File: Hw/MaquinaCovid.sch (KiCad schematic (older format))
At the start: 44 parts, among them J1 5 VCC, J10 Conn_01x04, J2 HC-SR04, J3 FTDI, J4 LCD, J5 MLX90614, J6 DS1307, J7 SD, J8 Power_supply, J9 Pines adicionales, Q1 2N2219, Q2 2N2219, SW1 RST, SW2 BOOT, SW3 SW_Push, U1 AZ1084CD-5.0TRG1, U2 AP2114H-3.3TRG1, U3 ESP32-WROOM-32, U4 LTV-817, U5 LTV-817, Y1 UD2-3NU

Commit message: Schematic changes
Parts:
- added R? (x2): 3.3k, symbol Device:R
- Q1: value 2N2219 -> MMBT4403; symbol Transistor_BJT:2N2219 -> agroin:MMBT2222A
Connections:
- net +3V3: now also J2.1 (Pin_1), J3.4 (Pin_4), J5.1 (Pin_1), J6.5 (Pin_5), J7.5 (Pin_5), R?.1, R?.1
- net +5V: no longer J2.1 (Pin_1), J3.4 (Pin_4), J5.1 (Pin_1), J6.5 (Pin_5), J7.5 (Pin_5)
- net GND: now also Q1.2 (E); no longer Q1.1 (E)
- net SCL: now also R?.2
- net SDA: now also R?.2
- net at R1.1: now also Q1.1 (B); no longer Q1.2 (B)
- net DS: no longer names the net of J6.2 (Pin_2)
- net GPIO2: no longer names the net of U3.26 (IO4)
- net SQ: no longer names the net of J6.1 (Pin_1)
- no-connect marks 13 -> 16
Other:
- moved on the sheet: C5, D4, D5, D6, R2, R3, R5

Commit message: finished Schematic
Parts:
- removed J1: 5 VCC, TerminalBlock:TerminalBlock_bornier-2_P5.08mm, symbol Connector:Screw_Terminal_01x02
- removed J10: Conn_01x04, symbol Connector_Generic:Conn_01x03
- removed J8: Power_supply, symbol Connector_Generic:Conn_01x02
- removed J9: Pines adicionales, symbol Connector_Generic:Conn_01x10
- removed Q2: 2N2219, Package_TO_SOT_THT:TO-39-3, symbol Transistor_BJT:2N2219
- removed R5: 330, symbol Device:R
- added D8: FM4007W-W, agroin:F4007, symbol Device:D
- added J10, J11: Screw_Terminal_01x03, TerminalBlock:TerminalBlock_bornier-3_P5.08mm, symbol Connector:Screw_Terminal_01x03
- added J7: Screw_Terminal_01x02, TerminalBlock:TerminalBlock_bornier-2_P5.08mm, symbol Connector:Screw_Terminal_01x02
- added J8, J9: Screw_Terminal_01x11, TerminalBlock:TerminalBlock_bornier-6_P5.08mm, symbol Connector:Screw_Terminal_01x06
- added Q2, Q3: MMBT2222A, Package_TO_SOT_SMD:SOT-23, symbol Transistor_BJT:2N3055
- added R12: 1k, Resistor_SMD:R_0805_2012Metric_Pad1.15x1.40mm_HandSolder, symbol Device:R
- added R4: 330, Resistor_SMD:R_0805_2012Metric_Pad1.15x1.40mm_HandSolder, symbol Device:R
- added Y1: UD2-3NU, agroin:UD2-3NU, symbol agroin:UD2-3NU
- BZ1: footprint (none) -> agroin:Buzzer
- D1, D3: value D_Schottky -> SS24FL; footprint (none) -> Diode_SMD:D_SOD-123F
- D2: value D -> 1N4148; footprint (none) -> Diode_SMD:D_SOD-323
- D4, D5, D6: footprint (none) -> LED_THT:LED_D10.0mm
- D7: value D -> FM4007W-W; footprint (none) -> agroin:F4007
- J1: renamed from J2; footprint (none) -> Connector_PinHeader_2.54mm:PinHeader_1x04_P2.54mm_Vertical
- J2: renamed from J3; footprint (none) -> Connector_PinHeader_2.54mm:PinHeader_1x06_P2.54mm_Vertical
- J3: renamed from J4; footprint (none) -> Connector_PinHeader_2.54mm:PinHeader_1x04_P2.54mm_Vertical
- J4: renamed from J5; footprint (none) -> Connector_PinHeader_2.54mm:PinHeader_1x04_P2.54mm_Vertical
- J5: renamed from J6; footprint (none) -> Connector_PinHeader_2.54mm:PinHeader_1x06_P2.54mm_Vertical
- J6: renamed from J7; footprint (none) -> Connector_PinHeader_2.54mm:PinHeader_1x06_P2.54mm_Vertical
- Q1: value MMBT4403 -> MMBT2222A; footprint Package_TO_SOT_THT:TO-39-3 -> Package_TO_SOT_SMD:SOT-23
- R1, R2, R3: footprint (none) -> Resistor_SMD:R_0805_2012Metric_Pad1.15x1.40mm_HandSolder
- R10: renamed from R8; footprint (none) -> Resistor_SMD:R_0805_2012Metric_Pad1.15x1.40mm_HandSolder
- R11: renamed from R9; footprint (none) -> Resistor_SMD:R_0805_2012Metric_Pad1.15x1.40mm_HandSolder
- R13: renamed from R10; footprint (none) -> Resistor_SMD:R_0805_2012Metric_Pad1.15x1.40mm_HandSolder
- R6, R7: renamed from R?; footprint (none) -> Resistor_SMD:R_0805_2012Metric_Pad1.15x1.40mm_HandSolder
- R8: renamed from R6; footprint (none) -> Resistor_SMD:R_0805_2012Metric_Pad1.15x1.40mm_HandSolder
- R9: renamed from R7; footprint (none) -> Resistor_SMD:R_0805_2012Metric_Pad1.15x1.40mm_HandSolder
- SW3: value SW_Push -> Extra; footprint (none) -> Button_Switch_SMD:SW_SPST_TL3342; lscs# (none) -> C318893; manf# (none) -> TS-1185EC-C-D-B
- U4, U5: footprint Housings_DIP:DIP-4_W7.62mm -> Package_DIP:DIP-4_W7.62mm_Socket
- Y2: renamed from Y1; footprint (none) -> agroin:UD2-3NU
- renumbered R4 to R5
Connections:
- net +3V3: now also D8.1 (K), Y1.8 (C1); no longer J5.5 (Pin_5), J6.5 (Pin_5)
- net +5V: now also J5.5 (Pin_5), J6.5 (Pin_5), J8.1 (Pin_1)
- net GND: now also J7.2 (Pin_2), J8.2 (Pin_2), J9.3 (Pin_3), J9.5 (Pin_5), J9.6 (Pin_6), Q2.2 (E), Q3.2 (E)
- net GPIO: now also J9.1 (Pin_1)
- net L3: now also R4.1
- net OP1: now also J9.2 (Pin_2)
- net OP2: now also J9.4 (Pin_4)
- net PS: now also J7.1 (Pin_1)
- net RX2: now also J8.4 (Pin_4)
- net SCL: now also J8.6 (Pin_6)
- net SDA: now also J8.5 (Pin_5)
- net TX2: now also J8.3 (Pin_3)
- net Ry2: now reaches U3.26 (IO4)
- net Ry2: now also R12.2
- net at D7.2 (A), Y2.1 (C2): now also Q3.3 (C)
- net at R13.1: now also Q3.1 (B)
- net at D6.2 (A): now also R4.2
- net COM renamed COM1
- net COM1: now also J10.2 (Pin_2)
- net NC renamed NC1
- net NC1: now also J10.1 (Pin_1)
- net NO renamed NO1
- net NO1: now also J10.3 (Pin_3)
- net Ry renamed Ry1
- new net: D8.2 (A), Q2.3 (C), Y1.1 (C2)
- new net: Q2.1 (B), R12.1
- new net COM2: J11.2 (Pin_2), Y1.3 (Com), Y1.6 (Com2)
- new net NC2: J11.1 (Pin_1), Y1.2 (NC)
- new net NO2: J11.3 (Pin_3), Y1.5 (NA1)
- no-connect marks 16 -> 17

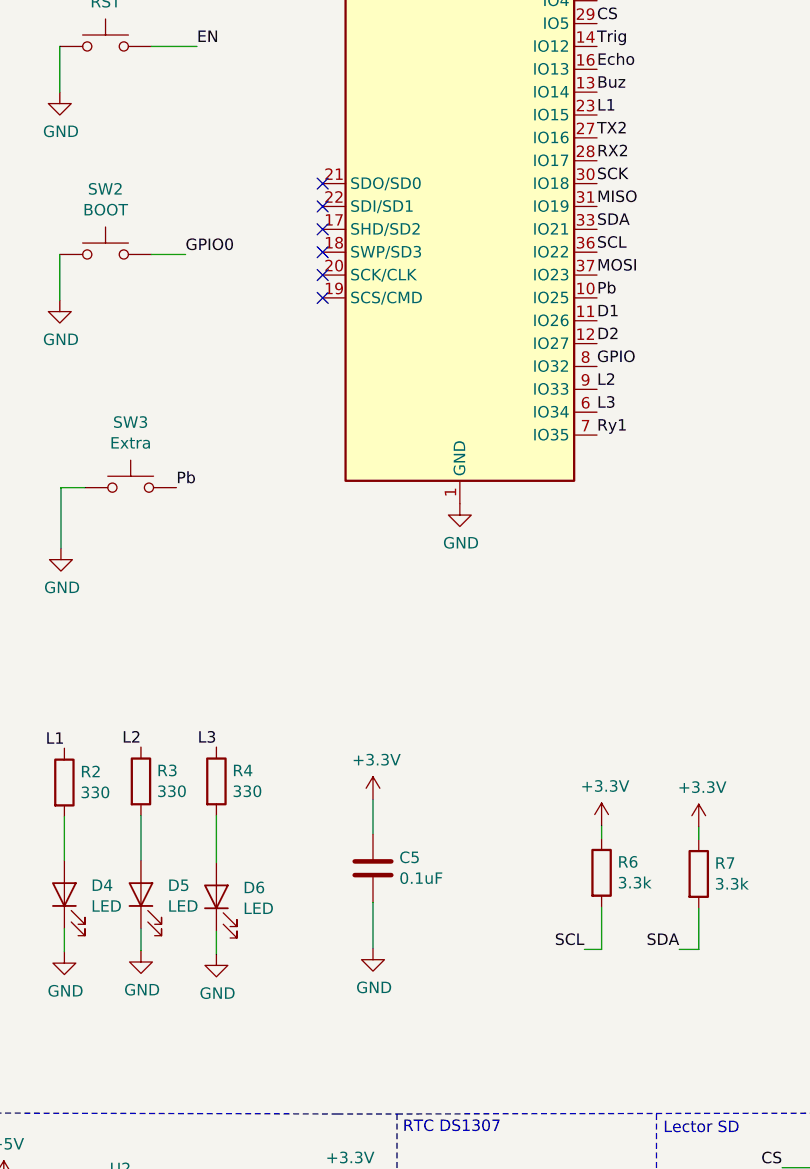
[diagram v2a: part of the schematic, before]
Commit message: Added led
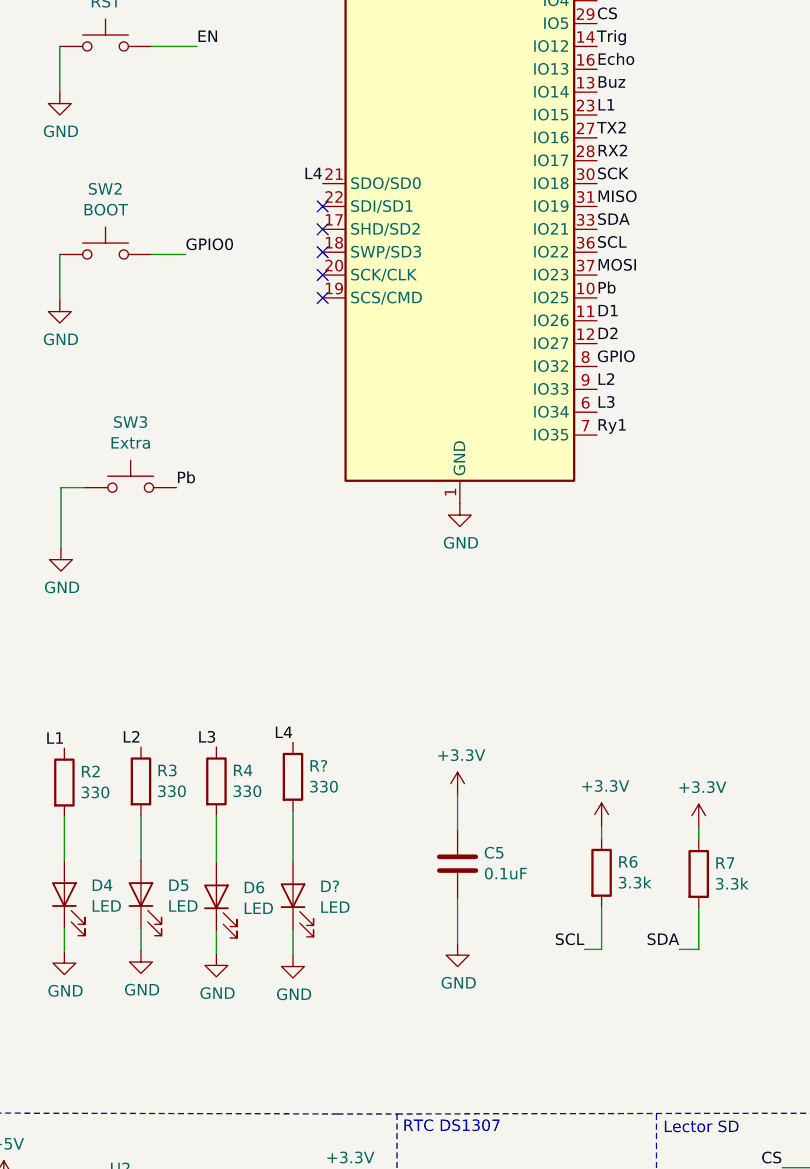
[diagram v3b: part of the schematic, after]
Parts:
- added D?: LED, LED_THT:LED_D10.0mm, symbol Device:LED
- added R?: 330, Resistor_SMD:R_0805_2012Metric_Pad1.15x1.40mm_HandSolder, symbol Device:R
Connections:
- net GND: now also D?.1 (K)
- net L4: now reaches U3.21 (SDO/SD0)
- net L4: now also R?.1
- new net: D?.2 (A), R?.2
- no-connect marks 17 -> 16
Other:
- moved on the sheet: C5
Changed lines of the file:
@@
 L Device:C C5
 U 1 1 5DFBF1D5
-P 4380 5605
-F 0 "C5" H 4495 5651 50  0000 L CNN
-F 1 "0.1uF" H 4495 5560 50  0000 L CNN
-F 2 "Capacitor_SMD:C_0805_2012Metric_Pad1.15x1.40mm_HandSolder" H 4418 5455 50  0001 C CNN
-F 3 "~" H 4380 5605 50  0001 C CNN
-F 4 "C376923" H -3690 3085 50  0001 C CNN "lscs#"
-F 5 "TCC0805X7R104K250DTS" H -3690 3085 50  0001 C CNN "manf#"
-	1    4380 5605
+P 4750 5585
+F 0 "C5" H 4865 5631 50  0000 L CNN
+F 1 "0.1uF" H 4865 5540 50  0000 L CNN
+F 2 "Capacitor_SMD:C_0805_2012Metric_Pad1.15x1.40mm_HandSolder" H 4788 5435 50  0001 C CNN
+F 3 "~" H 4750 5585 50  0001 C CNN
+F 4 "C376923" H -3320 3065 50  0001 C CNN "lscs#"
+F 5 "TCC0805X7R104K250DTS" H -3320 3065 50  0001 C CNN "manf#"
+	1    4750 5585
 	1    0    0    -1
 $EndComp
@@
 L power:GND #PWR025
 U 1 1 5DFBF1E1
-P 4380 5955
-F 0 "#PWR025" H 4380 5705 50  0001 C CNN
-F 1 "GND" H 4385 5782 50  0000 C CNN
-F 2 "" H 4380 5955 50  0001 C CNN
-F 3 "" H 4380 5955 50  0001 C CNN
-	1    4380 5955
-	1    0    0    -1
-$EndComp
-Wire Wire Line
-	4380 5755 4380 5955
-Wire Wire Line
-	4380 5455 4380 5305
+P 4750 5935
+F 0 "#PWR025" H 4750 5685 50  0001 C CNN
+F 1 "GND" H 4755 5762 50  0000 C CNN
+F 2 "" H 4750 5935 50  0001 C CNN
+F 3 "" H 4750 5935 50  0001 C CNN
+	1    4750 5935
+	1    0    0    -1
+$EndComp
+Wire Wire Line
+	4750 5735 4750 5935
+Wire Wire Line
+	4750 5435 4750 5285
 $Comp
 L power:+3.3V #PWR027
@@
 L power:+3.3V #PWR024
 U 1 1 5E03555F
-P 4380 5305
-F 0 "#PWR024" H 4380 5155 50  0001 C CNN
-F 1 "+3.3V" H 4395 5478 50  0000 C CNN
-F 2 "" H 4380 5305 50  0001 C CNN
-F 3 "" H 4380 5305 50  0001 C CNN
-	1    4380 5305
+P 4750 5285
+F 0 "#PWR024" H 4750 5135 50  0001 C CNN
+F 1 "+3.3V" H 4765 5458 50  0000 C CNN
+F 2 "" H 4750 5285 50  0001 C CNN
+F 3 "" H 4750 5285 50  0001 C CNN
+	1    4750 5285
 	1    0    0    -1
 $EndComp
@@
 ESP32
 NoConn ~ 5360 1610
-NoConn ~ 4160 2610
 $Comp
 L power:GND #PWR017
@@
 Wire Wire Line
 	8915 2910 8840 2910
+$Comp
+L Device:R R?
+U 1 1 5F0DC3AE
+P 4030 5205
+F 0 "R?" H 4100 5251 50  0000 L CNN
+F 1 "330" H 4100 5160 50  0000 L CNN
+F 2 "Resistor_SMD:R_0805_2012Metric_Pad1.15x1.40mm_HandSolder" V 3960 5205 50  0001 C CNN
+F 3 "~" H 4030 5205 50  0001 C CNN
+	1    4030 5205
+	1    0    0    -1
+$EndComp
+$Comp
+L Device:LED D?
+U 1 1 5F0DCDF6
+P 4030 5725
+F 0 "D?" V 4069 5608 50  0000 R CNN
+F 1 "LED" V 3978 5608 50  0000 R CNN
+F 2 "LED_THT:LED_D10.0mm" H 4030 5725 50  0001 C CNN
+F 3 "~" H 4030 5725 50  0001 C CNN
+	1    4030 5725
+	0    -1   -1   0
+$EndComp
+Wire Wire Line
+	4030 5355 4030 5575
+$Comp
+L power:GND #PWR?
+U 1 1 5F0E3D15
+P 4030 5985
+F 0 "#PWR?" H 4030 5735 50  0001 C CNN
+F 1 "GND" H 4035 5812 50  0000 C CNN
+F 2 "" H 4030 5985 50  0001 C CNN
+F 3 "" H 4030 5985 50  0001 C CNN
+	1    4030 5985
+	1    0    0    -1
+$EndComp
+Wire Wire Line
+	4030 5985 4030 5875
+Text Label 4030 5055 2    50   ~ 0
+L4
+Text Label 4160 2610 2    50   ~ 0
+L4
 $EndSCHEMATC

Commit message: Footprint placement (part 1)
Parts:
- added H1, H2, H3, H4: MountingHole, MountingHole:MountingHole_3.2mm_M3_Pad_Via, symbol Mechanical:MountingHole
- D7: renamed from D?; footprint LED_THT:LED_D10.0mm -> LED_SMD:LED_0805_2012Metric_Pad1.15x1.40mm_HandSolder
- J5: footprint Connector_PinHeader_2.54mm:PinHeader_1x06_P2.54mm_Vertical -> Connector_PinHeader_2.54mm:PinHeader_1x05_P2.54mm_Vertical; symbol Connector_Generic:Conn_01x06 -> Connector_Generic:Conn_01x05
- gave numbers to parts that had none: 1
- renumbered D7 to D8, D8 to D9, R9 to R10, R10 to R11, R11 to R12, R12 to R13, R13 to R14, R6 to R7, R7 to R8, R8 to R9
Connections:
- net +5V: now also J5.4 (Pin_4); no longer J5.5 (Pin_5)
- net D1: now also U3.8 (IO32); no longer U3.11 (IO26)
- net D2: now also U3.7 (IO35); no longer U3.12 (IO27)
- net GND: now also J5.5 (Pin_5), J7.1 (Pin_1); no longer J5.6 (Pin_6), J7.2 (Pin_2)
- net GPIO: now also U3.9 (IO33); no longer U3.8 (IO32)
- net L2: now also U3.11 (IO26); no longer U3.9 (IO33)
- net L3: now also U3.10 (IO25); no longer U3.6 (IO34)
- net PS: now also J7.2 (Pin_2); no longer J7.1 (Pin_1)
- net Pb: now also U3.6 (IO34); no longer U3.10 (IO25)
- net Ry1: now also U3.12 (IO27); no longer U3.7 (IO35)
- net Ry2: now also U3.17 (SHD/SD2); no longer U3.26 (IO4)
- net SCL: now also J5.2 (Pin_2); no longer J5.3 (Pin_3)
- net SDA: now also J5.3 (Pin_3); no longer J5.4 (Pin_4)
- no-connect marks 16 -> 14

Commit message: Finished PCB
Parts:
- added H5: MountingHole, MountingHole:MountingHole_3.2mm_M3_Pad_Via, symbol Mechanical:MountingHole
- D4, D5, D6: footprint LED_THT:LED_D10.0mm -> Connector_PinHeader_2.54mm:PinHeader_1x02_P2.54mm_Vertical
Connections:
- net +5V: now also J8.6 (Pin_6); no longer J8.1 (Pin_1)
- net Buz: now also U3.18 (SWP/SD3); no longer U3.13 (IO14)
- net Echo: now also U3.11 (IO26); no longer U3.16 (IO13)
- net GND: now also J8.5 (Pin_5); no longer J8.2 (Pin_2)
- net L1: now also U3.12 (IO27); no longer U3.23 (IO15)
- net L2: now also U3.13 (IO14); no longer U3.11 (IO26)
- net L3: now also U3.14 (IO12); no longer U3.10 (IO25)
- net RX2: now also J8.3 (Pin_3); no longer J8.4 (Pin_4)
- net Ry1: now also U3.16 (IO13); no longer U3.12 (IO27)
- net SCL: now also J8.1 (Pin_1); no longer J8.6 (Pin_6)
- net SDA: now also J8.2 (Pin_2); no longer J8.5 (Pin_5)
- net TX2: now also J8.4 (Pin_4); no longer J8.3 (Pin_3)
- net Trig: now also U3.10 (IO25); no longer U3.14 (IO12)
- no-connect marks 14 -> 15
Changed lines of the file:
@@
 L power:+5V #PWR041
 U 1 1 5E9F5A60
-P 7125 2130
-F 0 "#PWR041" H 7125 1980 50  0001 C CNN
-F 1 "+5V" H 7125 2275 50  0000 C CNN
-F 2 "" H 7125 2130 50  0001 C CNN
-F 3 "" H 7125 2130 50  0001 C CNN
-	1    7125 2130
+P 6750 2585
+F 0 "#PWR041" H 6750 2435 50  0001 C CNN
+F 1 "+5V" H 6750 2730 50  0000 C CNN
+F 2 "" H 6750 2585 50  0001 C CNN
+F 3 "" H 6750 2585 50  0001 C CNN
+	1    6750 2585
 	1    0    0    -1
 $EndComp
@@
 	1    0    0    -1
 $EndComp
-$Comp
-L Device:LED D4
-U 1 1 5F0990D7
-P 3030 5720
-F 0 "D4" V 3069 5603 50  0000 R CNN
-F 1 "LED" V 2978 5603 50  0000 R CNN
-F 2 "LED_THT:LED_D10.0mm" H 3030 5720 50  0001 C CNN
-F 3 "~" H 3030 5720 50  0001 C CNN
-	1    3030 5720
-	0    -1   -1   0
-$EndComp
-$Comp
-L Device:LED D5
-U 1 1 5F09A387
-P 3365 5720
-F 0 "D5" V 3404 5603 50  0000 R CNN
-F 1 "LED" V 3313 5603 50  0000 R CNN
-F 2 "LED_THT:LED_D10.0mm" H 3365 5720 50  0001 C CNN
-F 3 "~" H 3365 5720 50  0001 C CNN
-	1    3365 5720
-	0    -1   -1   0
-$EndComp
-$Comp
-L Device:LED D6
-U 1 1 5F09AFE6
-P 3695 5730
-F 0 "D6" V 3734 5613 50  0000 R CNN
-F 1 "LED" V 3643 5613 50  0000 R CNN
-F 2 "LED_THT:LED_D10.0mm" H 3695 5730 50  0001 C CNN
-F 3 "~" H 3695 5730 50  0001 C CNN
-	1    3695 5730
-	0    -1   -1   0
-$EndComp
 Wire Wire Line
 	3030 5570 3030 5380
-Wire Wire Line
-	3365 5570 3365 5375
 Wire Wire Line
 	3695 5580 3695 5375
@@
 NoConn ~ 4160 3110
 NoConn ~ 4160 3010
-NoConn ~ 4160 2910
+NoConn ~ 5360 1810
 NoConn ~ 4160 2710
 $Comp
@@
 L power:GND #PWR038
 U 1 1 5F0D3E19
-P 6900 2365
-F 0 "#PWR038" H 6900 2115 50  0001 C CNN
-F 1 "GND" H 6905 2192 50  0000 C CNN
-F 2 "" H 6900 2365 50  0001 C CNN
-F 3 "" H 6900 2365 50  0001 C CNN
-	1    6900 2365
-	1    0    0    -1
+P 7000 2590
+F 0 "#PWR038" H 7000 2340 50  0001 C CNN
+F 1 "GND" H 7005 2417 50  0000 C CNN
+F 2 "" H 7000 2590 50  0001 C CNN
+F 3 "" H 7000 2590 50  0001 C CNN
+	1    7000 2590
+	0    1    1    0
 $EndComp
 $Comp
@@
 	1    0    0    -1
 $EndComp
+Text Label 7200 2490 2    50   ~ 0
+TX2
 Text Label 7200 2390 2    50   ~ 0
-TX2
-Text Label 7200 2490 2    50   ~ 0
 RX2
-Text Label 7200 2590 2    50   ~ 0
+Text Label 7200 2290 2    50   ~ 0
 SDA
-Text Label 7200 2690 2    50   ~ 0
+Text Label 7200 2190 2    50   ~ 0
 SCL
 Text Label 7195 4925 2    50   ~ 0
@@
 Text Label 7200 3105 2    50   ~ 0
 OP2
-Wire Wire Line
-	7200 2290 6900 2290
-Wire Wire Line
-	6900 2290 6900 2365
 Text Label 7200 2805 2    50   ~ 0
 GPIO
@@
 	1    0    0    -1
 $EndComp
-Text Label 5360 2010 0    50   ~ 0
+Text Label 5360 3110 0    50   ~ 0
 Trig
-Text Label 5360 2110 0    50   ~ 0
+Text Label 5360 3210 0    50   ~ 0
 Echo
 Text Label 945  3070 2    50   ~ 0
 Buz
-Text Label 5360 2210 0    50   ~ 0
+Text Label 4160 2910 2    50   ~ 0
 Buz
 Text Label 8090 4670 0    50   ~ 0
@@
 Text Label 3695 5075 2    50   ~ 0
 L3
-Text Label 5360 2310 0    50   ~ 0
+Text Label 5360 3310 0    50   ~ 0
 L1
-Text Label 5360 3210 0    50   ~ 0
+Text Label 5360 2210 0    50   ~ 0
 L2
-Text Label 5360 3110 0    50   ~ 0
+Text Label 5360 2010 0    50   ~ 0
 L3
 Text Label 5360 3410 0    50   ~ 0
@@
 RX2
 NoConn ~ 1705 1015
-Text Label 5360 3310 0    50   ~ 0
+Text Label 5360 2110 0    50   ~ 0
 Ry1
 $Comp
@@
 	1    0    0    -1
 $EndComp
-Wire Wire Line
-	7200 2190 7125 2190
-Wire Wire Line
-	7125 2190 7125 2130
 $Comp
 L power:GND #PWR042
@@
 Wire Wire Line
 	6960 1035 6960 1225
+Wire Wire Line
+	3365 5375 3365 5570
+$Comp
+L Device:LED D4
+U 1 1 5F214149
+P 3030 5720
+F 0 "D4" V 3069 5603 50  0000 R CNN
+F 1 "LED" V 2978 5603 50  0000 R CNN
+F 2 "Connector_PinHeader_2.54mm:PinHeader_1x02_P2.54mm_Vertical" H 3030 5720 50  0001 C CNN
+F 3 "~" H 3030 5720 50  0001 C CNN
+	1    3030 5720
+	0    -1   -1   0
+$EndComp
+$Comp
+L Device:LED D5
+U 1 1 5F216C39
+P 3365 5720
+F 0 "D5" V 3404 5603 50  0000 R CNN
+F 1 "LED" V 3313 5603 50  0000 R CNN
+F 2 "Connector_PinHeader_2.54mm:PinHeader_1x02_P2.54mm_Vertical" H 3365 5720 50  0001 C CNN
+F 3 "~" H 3365 5720 50  0001 C CNN
+	1    3365 5720
+	0    -1   -1   0
+$EndComp
+$Comp
+L Device:LED D6
+U 1 1 5F2170D6
+P 3695 5730
+F 0 "D6" V 3734 5613 50  0000 R CNN
+F 1 "LED" V 3643 5613 50  0000 R CNN
+F 2 "Connector_PinHeader_2.54mm:PinHeader_1x02_P2.54mm_Vertical" H 3695 5730 50  0001 C CNN
+F 3 "~" H 3695 5730 50  0001 C CNN
+	1    3695 5730
+	0    -1   -1   0
+$EndComp
+NoConn ~ 5360 2310
+Wire Wire Line
+	7200 2690 6750 2690
+Wire Wire Line
+	6750 2585 6750 2690
+Wire Wire Line
+	7000 2590 7200 2590
+$Comp
+L Mechanical:MountingHole H5
+U 1 1 5F5898FA
+P 5720 3715
+F 0 "H5" H 5820 3761 50  0000 L CNN
+F 1 "MountingHole" H 5820 3670 50  0000 L CNN
+F 2 "MountingHole:MountingHole_3.2mm_M3_Pad_Via" H 5720 3715 50  0001 C CNN
+F 3 "~" H 5720 3715 50  0001 C CNN
+	1    5720 3715
+	1    0    0    -1
+$EndComp
 $EndSCHEMATC
